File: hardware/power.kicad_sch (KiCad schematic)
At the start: 3 parts, among them IC2 TPS54202HDDCR

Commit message: XTR117 Output
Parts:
- removed C1: C, symbol Device:C
- removed IC2: TPS54202HDDCR, Samacsys:SOT95P280X110-6N, symbol Samacsys:TPS54202HDDCR
- removed L1: L_Ferrite, symbol Device:L_Ferrite

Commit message: Almost everything
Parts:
- added C11, C15: 0.1uF, symbol Device:C
- added C12, C16, C17, C18: 10uF, symbol Device:C
- added C13, C14: 2.2uF, symbol Device:C
- added D2: D_Schottky, symbol Device:D_Schottky
- added L1: 8.2uH, symbol Device:L
- added L2: 4.7uH, symbol Device:L
- added R23, R25: 100R, symbol Device:R
- added R24: 5.23R, symbol Device:R
- added R26: 13.7R, symbol Device:R
- added U15, U16, U17, U18, U19, U20: KF301-5.0-2P, EasyEDA:CONN-TH_P5.00_KF301-5.0-2P, symbol EasyEDA:KF301-5.0-2P
- added U21, U22: LMR51420YFDDCR, EasyEDA:SOT-23-6_L2.9-W1.6-P0.95-LS2.8-BL, symbol EasyEDA:LMR51420YFDDCR
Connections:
- new net: C11.1, U22.6 (CB)
- new net: R25.2, R26.1, U21.4 (FB)
- new net: C15.1, U21.6 (CB)
- new net: R23.2, R24.1, U22.4 (FB)
- new net +12V: C12.1, C17.1, L1.2, R23.1
- new net +24V: C13.2, C14.2, U15.1, U15.2, U16.1, U16.2, U17.1, U17.2, U21.3 (VIN), U21.5 (EN), U22.3 (VIN), U22.5 (EN)
- new net +5V: C16.1, C18.1, D2.2 (A), L2.2, R25.1
- new net 12V_SW: C11.2, L1.1, U22.2 (SW)
- new net 5V_SW: C15.2, L2.1, U21.2 (SW)
- new net GND: C12.2, C13.1, C14.1, C16.2, C17.2, C18.2, R24.2, R26.2, U18.1, U18.2, U19.1, U19.2, U20.1, U20.2, U21.1 (GND), U22.1 (GND)
- new net VSYS: D2.1 (K)

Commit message: Board complete
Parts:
- removed D2: D_Schottky, symbol Device:D_Schottky
- removed U15, U16, U17, U18, U19, U20: KF301-5.0-2P, EasyEDA:CONN-TH_P5.00_KF301-5.0-2P, symbol EasyEDA:KF301-5.0-2P
- removed U21, U22: LMR51420YFDDCR, EasyEDA:SOT-23-6_L2.9-W1.6-P0.95-LS2.8-BL, symbol EasyEDA:LMR51420YFDDCR
- added IC3: LMR51420XFDDCR, Samacsys:SOT95P280X110-6N, symbol Samacsys:LMR51420XFDDCR
- added J3, J4: TB006-508-03BE, Samacsys:TB00650803BE, symbol Samacsys:TB006-508-03BE
- added J5: TB007-508-02BE, Samacsys:TB00750802BE, symbol Samacsys:TB007-508-02BE
- added PS1: LMR51420YFDDCR, Samacsys:SOT95P280X110-6N, symbol Samacsys:LMR51420YFDDCR
- added TP1: TP_+12V, TestPoint:TestPoint_THTPad_2.0x2.0mm_Drill1.0mm, symbol Connector:TestPoint
- added TP2, TP4, TP6, TP7: GND_TP, TestPoint:TestPoint_THTPad_D2.0mm_Drill1.0mm, symbol Connector:TestPoint
- added TP3: TP_+5V, TestPoint:TestPoint_THTPad_2.0x2.0mm_Drill1.0mm, symbol Connector:TestPoint
- added TP5: TP_+24V, TestPoint:TestPoint_THTPad_2.0x2.0mm_Drill1.0mm, symbol Connector:TestPoint
- C1: renamed from C13; footprint (none) -> Capacitor_SMD:C_1206_3216Metric_Pad1.33x1.80mm_HandSolder
- C2: renamed from C14; footprint (none) -> Capacitor_SMD:C_1206_3216Metric_Pad1.33x1.80mm_HandSolder
- C3: renamed from C11; footprint (none) -> Capacitor_SMD:C_1206_3216Metric_Pad1.33x1.80mm_HandSolder
- C4: renamed from C15; footprint (none) -> Capacitor_SMD:C_1206_3216Metric_Pad1.33x1.80mm_HandSolder
- C5: renamed from C12; value 10uF -> 22uF; footprint (none) -> Capacitor_SMD:C_1206_3216Metric_Pad1.33x1.80mm_HandSolder
- C6: renamed from C16; footprint (none) -> Capacitor_SMD:C_1206_3216Metric_Pad1.33x1.80mm_HandSolder
- C7: renamed from C17; value 10uF -> 22uF; footprint (none) -> Capacitor_SMD:C_1206_3216Metric_Pad1.33x1.80mm_HandSolder
- C8: renamed from C18; footprint (none) -> Capacitor_SMD:C_1206_3216Metric_Pad1.33x1.80mm_HandSolder
- L1: value 8.2uH -> 22uH; footprint (none) -> Samacsys:INDPM7070X480N
- L2: footprint (none) -> Samacsys:INDC3225X120N
- R1: renamed from R23; value 100R -> 100k; footprint (none) -> Resistor_SMD:R_1206_3216Metric_Pad1.30x1.75mm_HandSolder
- R2: renamed from R24; value 5.23R -> 5.23k; footprint (none) -> Resistor_SMD:R_1206_3216Metric_Pad1.30x1.75mm_HandSolder
- R3: renamed from R25; value 100R -> 100k; footprint (none) -> Resistor_SMD:R_1206_3216Metric_Pad1.30x1.75mm_HandSolder
- R4: renamed from R26; value 13.7R -> 13.7k; footprint (none) -> Resistor_SMD:R_1206_3216Metric_Pad1.30x1.75mm_HandSolder
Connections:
- net +12V: now also TP1.1
- net +24V: now also IC3.3 (VIN), IC3.5 (EN), J3.1, J3.2, J3.3, J5.1, PS1.3 (VIN), PS1.5 (EN), TP5.1
- net +5V: now also TP3.1
- net 12V_SW: now also IC3.2 (SW)
- net 5V_SW: now also PS1.2 (SW)
- net GND: now also IC3.1 (GND), J4.1, J4.2, J4.3, J5.2, PS1.1 (GND), TP2.1, TP4.1, TP6.1, TP7.1
- net at C3.1: now also IC3.6 (CB)
- net at R3.2, R4.1: now also PS1.4 (FB)
- net at C4.1: now also PS1.6 (CB)
- net at R1.2, R2.1: now also IC3.4 (FB)
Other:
- note added: "1.1MHz"
- note added: "500kHz"
- note added: "MAIN BOARD SUPPLY PINS"
- moved on the sheet: C1, C2, C3, C4, C5, C6, C7, C8, L1, L2, R1, R2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

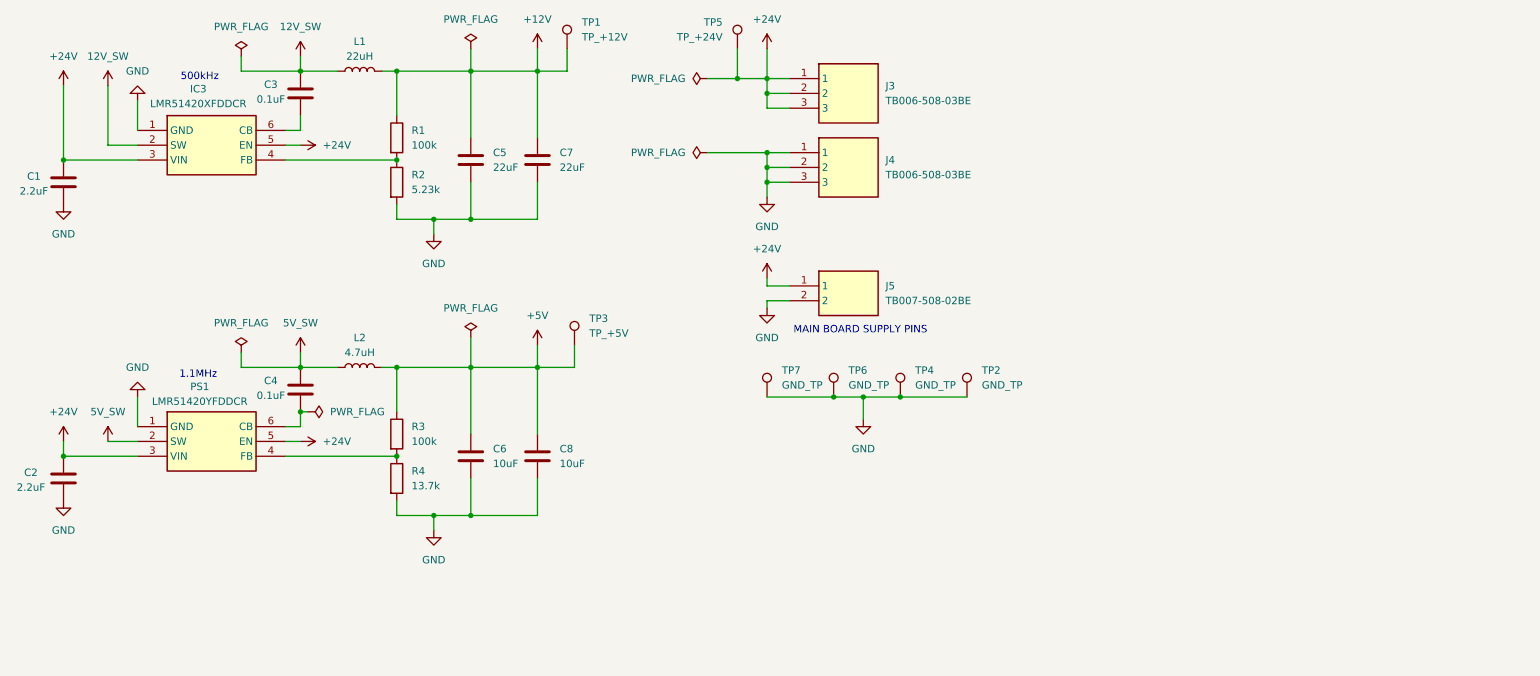
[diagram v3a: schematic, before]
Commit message: Modbus, small schematic changes
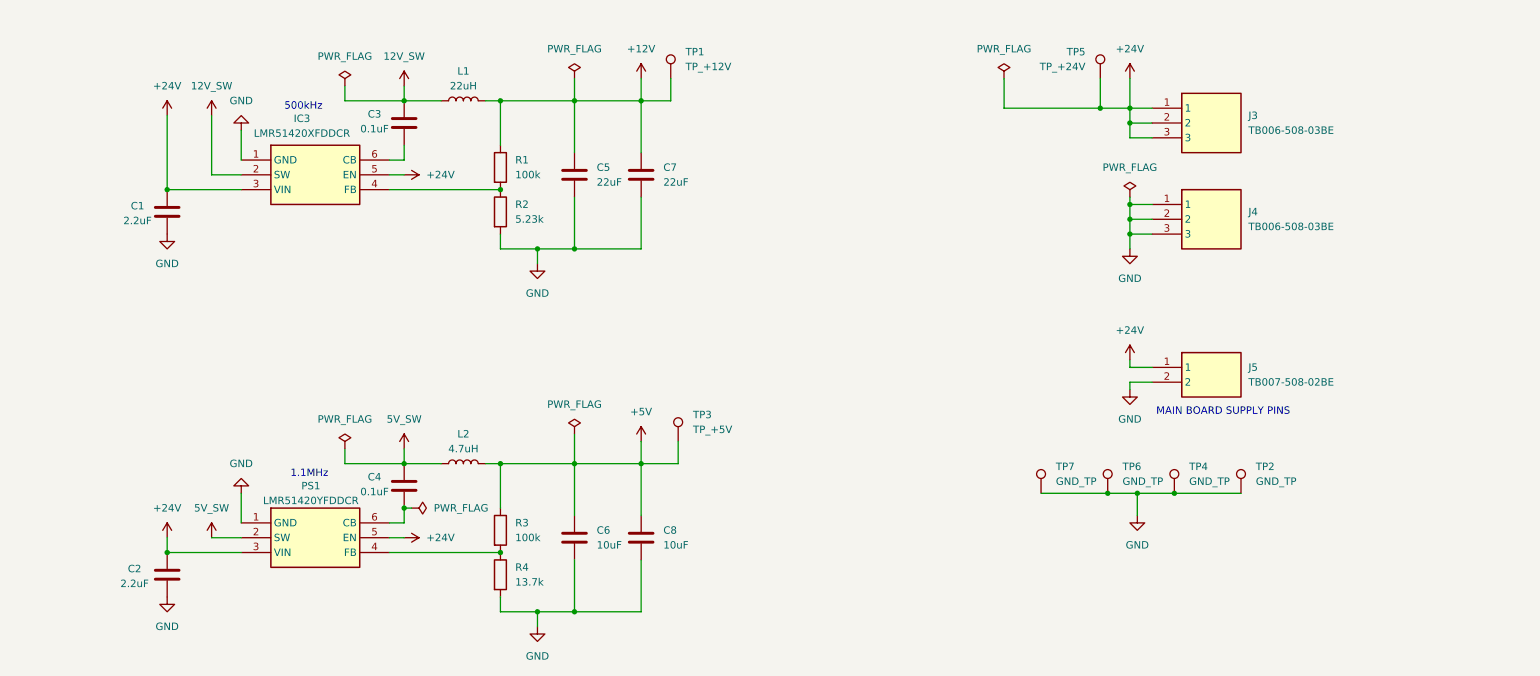
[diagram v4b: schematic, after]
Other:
- moved on the sheet: C1, C2, C3, C4, C5, C6, C7, C8, IC3, J3, J4, J5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

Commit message: Modbus library done
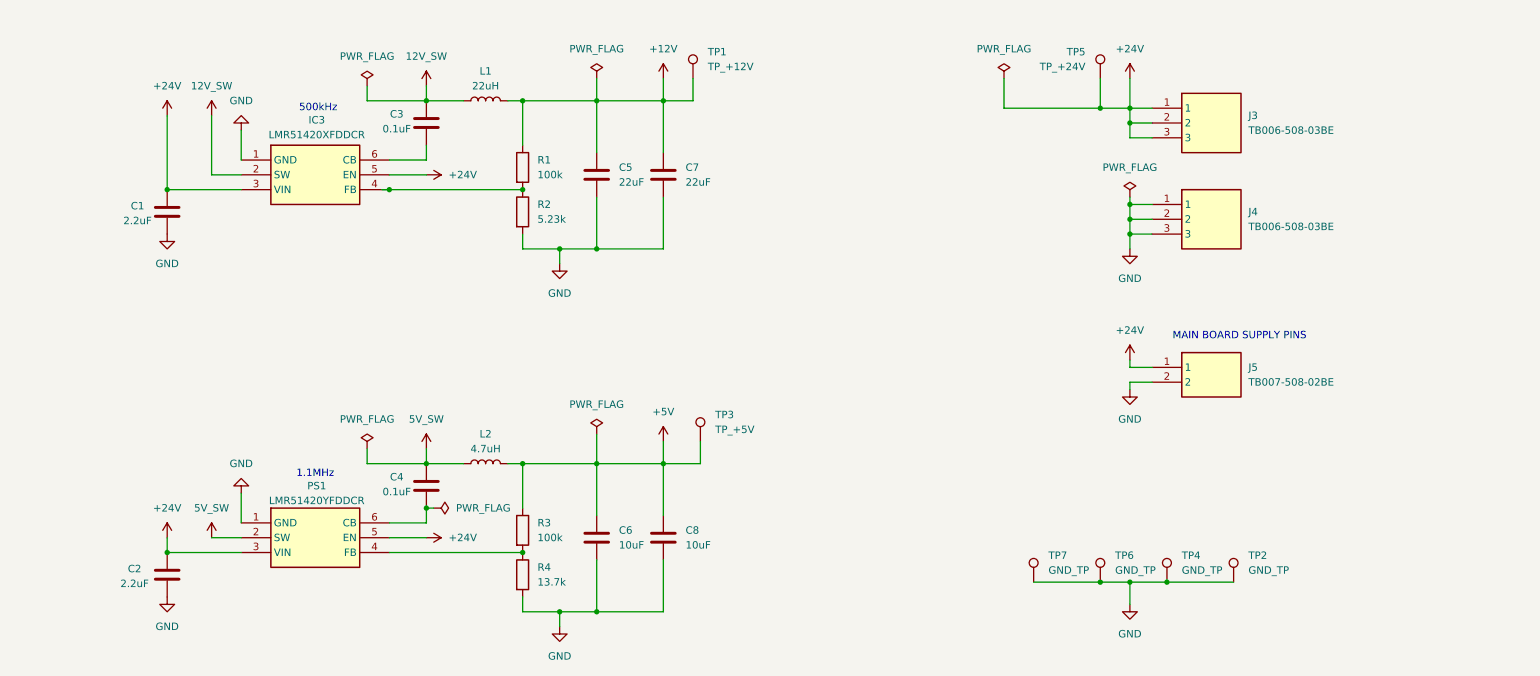
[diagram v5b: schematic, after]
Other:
- moved on the sheet: C3, C4, C5, C6, C7, C8, L1, L2, R1, R2, R3, R4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

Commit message: UART parity and better timing handling
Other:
- title: (none) -> Power Supply
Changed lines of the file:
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@@
 	(generator_version "9.0")
 	(paper "A4")
+	(title_block
+		(title "Power Supply")
+	)
 	(text "500kHz"
 		(exclude_from_sim no)
